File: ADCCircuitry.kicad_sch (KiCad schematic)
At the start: 24 parts, among them J1 Screw_Terminal_01x04, J2 Screw_Terminal_01x04, J3 Screw_Terminal_01x04, J4 Screw_Terminal_01x04, U2 ADS112C04, U3 ADS112C04, U4 ADS112C04, U5 ADS112C04

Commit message: Add SAFE +24V
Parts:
- J1, J2, J3, J4: Digikey PN (none) -> ED10563-ND
- TP1, TP2, TP3, TP4: footprint (none) -> TestPoint:TestPoint_Pad_D2.0mm
- U2, U3, U4, U5: LCSC (none) -> C701615; MPN (none) -> ADS112C04IPWR
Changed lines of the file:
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@@
 			)
 		)
-		(property "Footprint" ""
+		(property "Footprint" "TestPoint:TestPoint_Pad_D2.0mm"
 			(at 62.23 115.57 0)
 			(effects
@@
 			)
 		)
+		(property "Digikey PN" "ED10563-ND"
+			(at 201.93 40.64 0)
+			(effects
+				(font
+					(size 1.27 1.27)
+				)
+				(hide yes)
+			)
+		)
 		(pin "2"
 		)
@@
 			)
 		)
-		(property "Footprint" ""
+		(property "Footprint" "TestPoint:TestPoint_Pad_D2.0mm"
 			(at 62.23 64.77 0)
 			(effects
@@
 			)
 		)
-		(property "Footprint" ""
+		(property "Footprint" "TestPoint:TestPoint_Pad_D2.0mm"
 			(at 184.15 115.57 0)
 			(effects
@@
 			)
 		)
+		(property "MPN" "ADS112C04IPWR"
+			(at 99.06 134.62 0)
+			(effects
+				(font
+					(size 1.27 1.27)
+				)
+				(hide yes)
+			)
+		)
+		(property "LCSC" "C701615"
+			(at 99.06 134.62 0)
+			(effects
+				(font
+					(size 1.27 1.27)
+				)
+				(hide yes)
+			)
+		)
 		(property "ADC Number" "2"
 			(at 99.06 134.62 0)
@@
 			)
 		)
-		(property "Footprint" ""
+		(property "Footprint" "TestPoint:TestPoint_Pad_D2.0mm"
 			(at 184.15 64.77 0)
 			(effects
@@
 			)
 		)
+		(property "MPN" "ADS112C04IPWR"
+			(at 99.06 83.82 0)
+			(effects
+				(font
+					(size 1.27 1.27)
+				)
+				(hide yes)
+			)
+		)
+		(property "LCSC" "C701615"
+			(at 99.06 83.82 0)
+			(effects
+				(font
+					(size 1.27 1.27)
+				)
+				(hide yes)
+			)
+		)
 		(pin "2"
 		)
@@
 			)
 		)
+		(property "LCSC" "C701615"
+			(at 220.98 83.82 0)
+			(effects
+				(font
+					(size 1.27 1.27)
+				)
+				(hide yes)
+			)
+		)
+		(property "MPN" "ADS112C04IPWR"
+			(at 220.98 83.82 0)
+			(effects
+				(font
+					(size 1.27 1.27)
+				)
+				(hide yes)
+			)
+		)
 		(pin "2"
 		)
@@
 			)
 		)
+		(property "Digikey PN" "ED10563-ND"
+			(at 63.5 40.64 0)
+			(effects
+				(font
+					(size 1.27 1.27)
+				)
+				(hide yes)
+			)
+		)
 		(pin "2"
 		)
@@
 			)
 		)
+		(property "Digikey PN" "ED10563-ND"
+			(at 63.5 27.94 0)
+			(effects
+				(font
+					(size 1.27 1.27)
+				)
+				(hide yes)
+			)
+		)
 		(pin "2"
 		)
@@
 			)
 		)
+		(property "MPN" "ADS112C04IPWR"
+			(at 220.98 134.62 0)
+			(effects
+				(font
+					(size 1.27 1.27)
+				)
+				(hide yes)
+			)
+		)
+		(property "LCSC" "C701615"
+			(at 220.98 134.62 0)
+			(effects
+				(font
+					(size 1.27 1.27)
+				)
+				(hide yes)
+			)
+		)
 		(pin "2"
 		)
@@
 			(at 201.93 27.94 0)
 			(effects
+				(font
+					(size 1.27 1.27)
+				)
+				(hide yes)
+			)
+		)
+		(property "Digikey PN" "ED10563-ND"
+			(at 201.93 27.94 0)
+			(effects

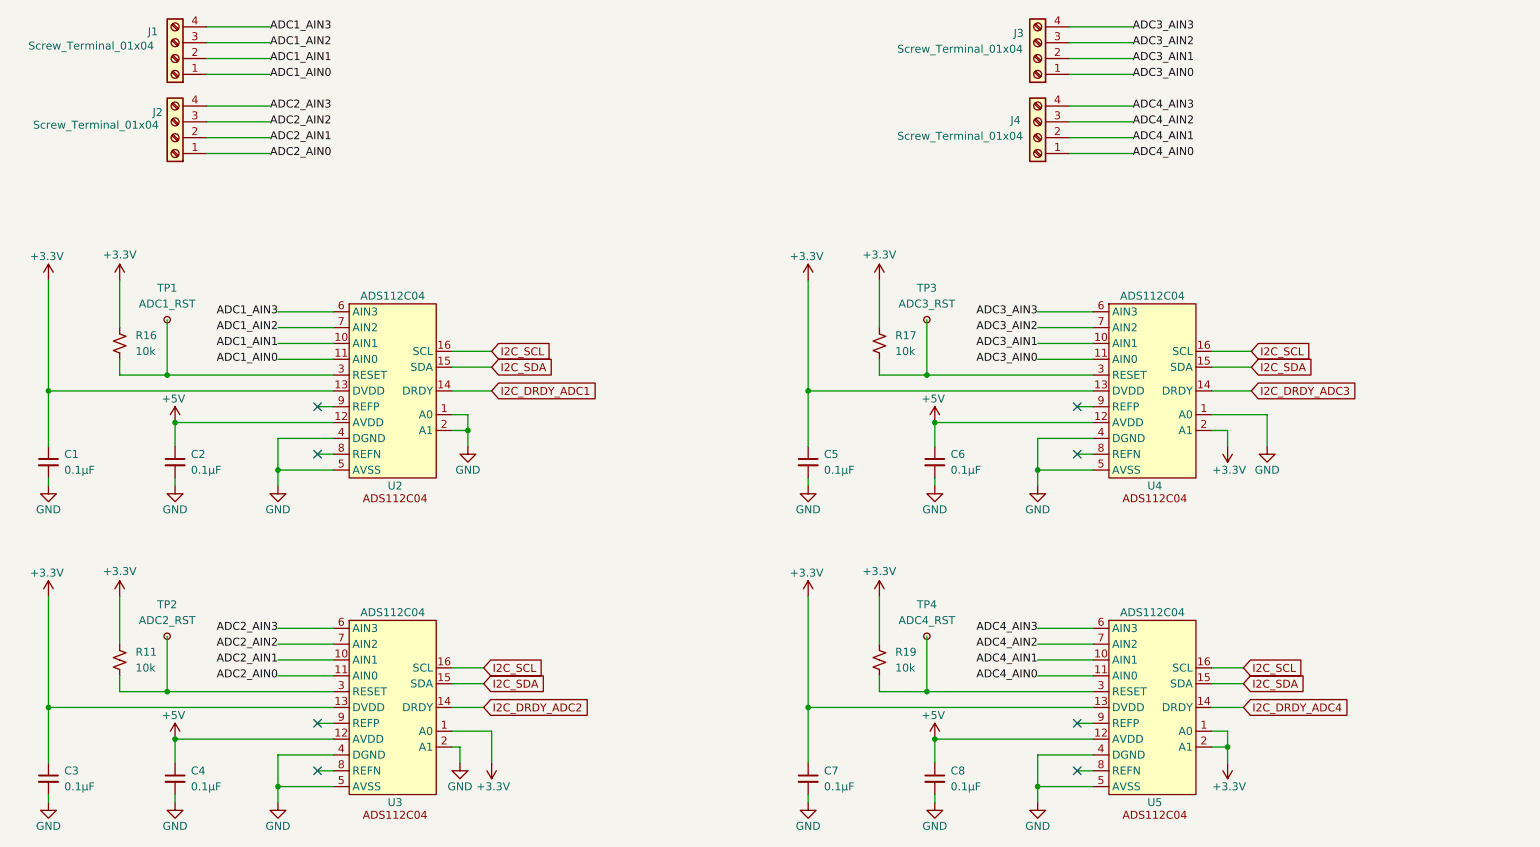
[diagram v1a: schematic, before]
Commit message: Add load cell inputs
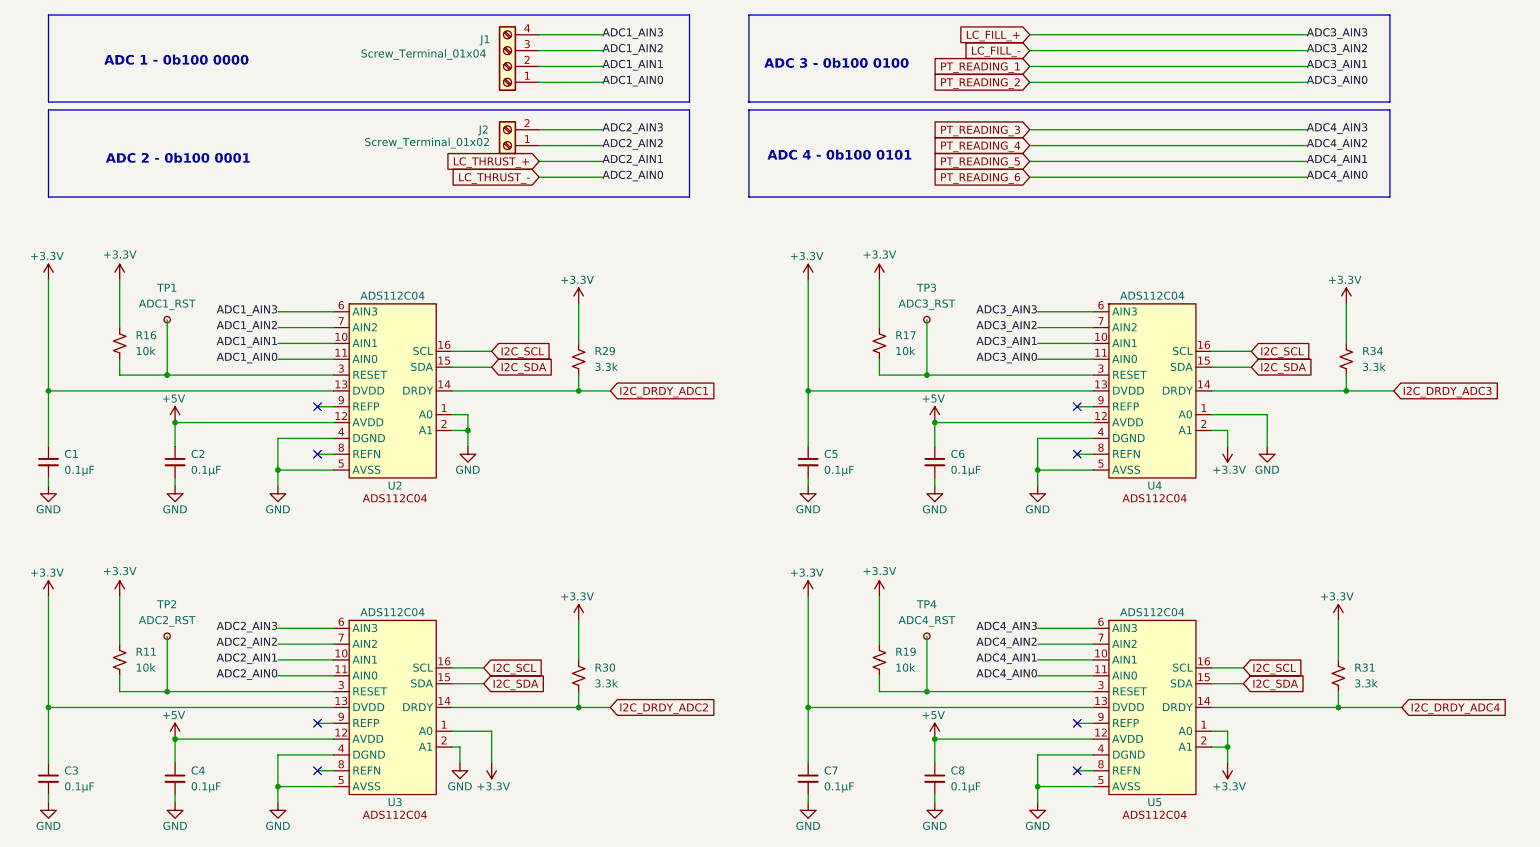
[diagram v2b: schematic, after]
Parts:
- removed J2, J3, J4: Screw_Terminal_01x04, TerminalBlock:TerminalBlock_Xinya_XY308-2.54-4P_1x04_P2.54mm_Horizontal, symbol Connector:Screw_Terminal_01x04
- added J2: Screw_Terminal_01x02, symbol Connector:Screw_Terminal_01x02
- added R29, R30, R31, R34: 3.3k, Resistor_SMD:R_0402_1005Metric, symbol Device:R_Small_US
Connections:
- net +3.3V: now also R29.1, R30.1, R31.1, R34.1
- net ADC2_AIN2: now also J2.1 (Pin_1)
- net ADC2_AIN3: now also J2.2 (Pin_2)
- net I2C_DRDY_ADC1: now also R29.2
- net I2C_DRDY_ADC2: now also R30.2
- net I2C_DRDY_ADC3: now also R34.2
- net I2C_DRDY_ADC4: now also R31.2
- net ADC2_AIN0 renamed LC_THRUST_-
- net ADC2_AIN1 renamed LC_THRUST_+
- net ADC3_AIN0 renamed PT_READING_2
- net ADC3_AIN1 renamed PT_READING_1
- net ADC3_AIN2 renamed LC_FILL_-
- net ADC3_AIN3 renamed LC_FILL_+
- net ADC4_AIN0 renamed PT_READING_6
- net ADC4_AIN1 renamed PT_READING_5
- net ADC4_AIN2 renamed PT_READING_4
- net ADC4_AIN3 renamed PT_READING_3
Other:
- note added: "ADC 1 - 0b100 0000"
- note added: "ADC 2 - 0b100 0001"
- note added: "ADC 3 - 0b100 0100"
- note added: "ADC 4 - 0b100 0101"
- moved on the sheet: J1

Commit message: v0.1 sch. Add devkit c1 footprint
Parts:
- J2: footprint (none) -> TerminalBlock:TerminalBlock_Xinya_XY308-2.54-2P_1x02_P2.54mm_Horizontal
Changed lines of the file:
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@@
 			)
 		)
-		(property "Footprint" ""
+		(property "Footprint" "TerminalBlock:TerminalBlock_Xinya_XY308-2.54-2P_1x02_P2.54mm_Horizontal"
 			(at 116.84 41.91 0)
 			(effects

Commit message: Add all footprints
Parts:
- U2, U3, U4, U5: footprint ADS112C04IPWR:SOP65P640X120-16N -> Package_SO:TSSOP-16_4.4x5mm_P0.65mm
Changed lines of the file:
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@@
 			)
 		)
-		(property "Footprint" "ADS112C04IPWR:SOP65P640X120-16N"
+		(property "Footprint" "Package_SO:TSSOP-16_4.4x5mm_P0.65mm"
 			(at 223.52 128.27 0)
 			(effects
@@
 			)
 		)
-		(property "Footprint" "ADS112C04IPWR:SOP65P640X120-16N"
+		(property "Footprint" "Package_SO:TSSOP-16_4.4x5mm_P0.65mm"
 			(at 223.52 77.47 0)
 			(effects
@@
 			)
 		)
-		(property "Footprint" "ADS112C04IPWR:SOP65P640X120-16N"
+		(property "Footprint" "Package_SO:TSSOP-16_4.4x5mm_P0.65mm"
 			(at 345.44 77.47 0)
 			(effects
@@
 			)
 		)
-		(property "Footprint" "ADS112C04IPWR:SOP65P640X120-16N"
+		(property "Footprint" "Package_SO:TSSOP-16_4.4x5mm_P0.65mm"
 			(at 345.44 128.27 0)
 			(effects

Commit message: Almost done routing
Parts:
- TP1, TP2, TP3, TP4: footprint TestPoint:TestPoint_Pad_D2.0mm -> TestPoint:TestPoint_Pad_D1.0mm
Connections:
- net PT_READING_3: now also U5.7 (AIN2); no longer U5.6 (AIN3)
- net PT_READING_4: now also U5.6 (AIN3); no longer U5.7 (AIN2)

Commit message: routing broken
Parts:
- removed TP1: ADC1_RST, TestPoint:TestPoint_Pad_D1.0mm, symbol Connector:TestPoint_Small
- removed TP2: ADC2_RST, TestPoint:TestPoint_Pad_D1.0mm, symbol Connector:TestPoint_Small
- removed TP3: ADC3_RST, TestPoint:TestPoint_Pad_D1.0mm, symbol Connector:TestPoint_Small
- removed TP4: ADC4_RST, TestPoint:TestPoint_Pad_D1.0mm, symbol Connector:TestPoint_Small
- renumbered C3 to C2, C2 to C3, C7 to C6, C6 to C7, J2 to J10, J1 to J9, R16 to R15, R11 to R16, R29 to R17, R30 to R18, R17 to R19, R19 to R20, R31 to R21, R34 to R22

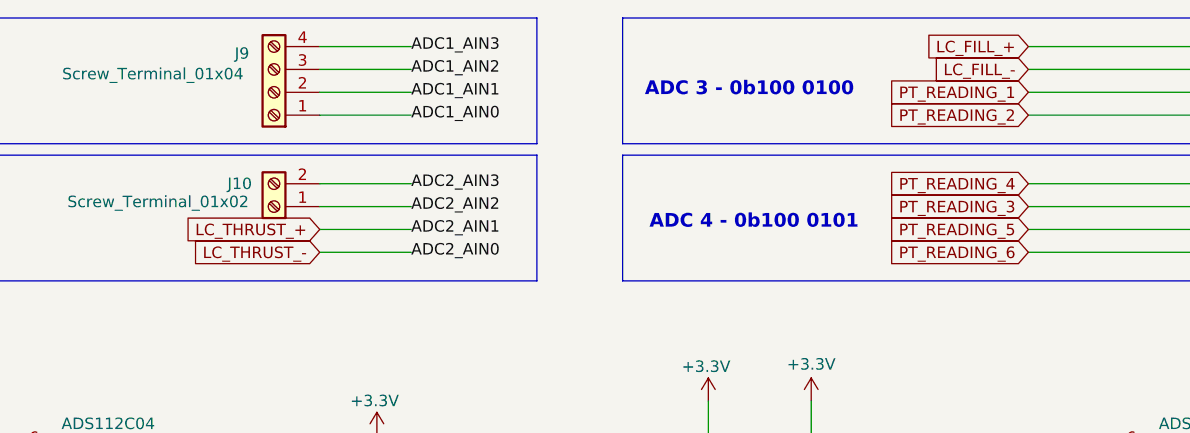
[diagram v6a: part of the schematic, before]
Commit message: Route power to sensors
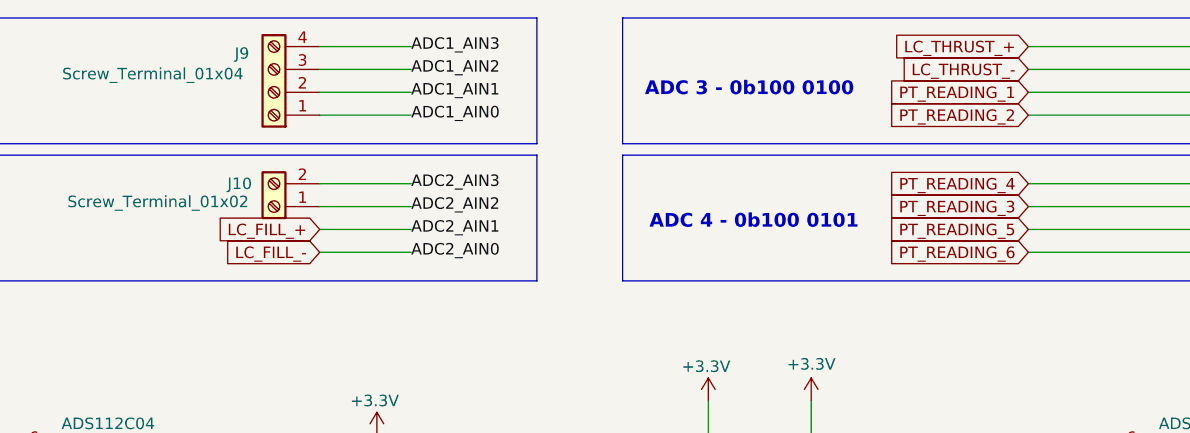
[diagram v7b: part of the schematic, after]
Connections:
- net LC_FILL_+: now also U3.10 (AIN1); no longer U4.6 (AIN3)
- net LC_FILL_-: now also U3.11 (AIN0); no longer U4.7 (AIN2)
- net LC_THRUST_+: now also U4.6 (AIN3); no longer U3.10 (AIN1)
- net LC_THRUST_-: now also U4.7 (AIN2); no longer U3.11 (AIN0)
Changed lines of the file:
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@@
+		)
+	)
+	(global_label "LC_THRUST_+"
+		(shape input)
+		(at 200.66 24.13 180)
+		(fields_autoplaced yes)
+		(effects
+			(font
+				(size 1.27 1.27)
+			)
+			(justify right)
+		)
+		(property "Intersheetrefs" "${INTERSHEET_REFS}"
+			(at 184.7934 24.13 0)
+			(effects
+				(font
+					(size 1.27 1.27)
+				)
+				(justify right)
+				(hide yes)
+			)
 		)
 	)
@@
 		)
 	)
-	(global_label "LC_THRUST_+"
+	(global_label "LC_THRUST_-"
+		(shape input)
+		(at 200.66 26.67 180)
+		(fields_autoplaced yes)
+		(effects
+			(font
+				(size 1.27 1.27)
+			)
+			(justify right)
+		)
+		(property "Intersheetrefs" "${INTERSHEET_REFS}"
+			(at 184.7934 26.67 0)
+			(effects
+				(font
+					(size 1.27 1.27)
+				)
+				(justify right)
+				(hide yes)
+			)
+		)
+	)
+	(global_label "LC_FILL_-"
+		(shape input)
+		(at 121.92 46.99 180)
+		(fields_autoplaced yes)
+		(effects
+			(font
+				(size 1.27 1.27)
+			)
+			(justify right)
+		)
+		(property "Intersheetrefs" "${INTERSHEET_REFS}"
+			(at 109.3795 46.99 0)
+			(effects
+				(font
+					(size 1.27 1.27)
+				)
+				(justify right)
+				(hide yes)
+			)
+		)
+	)
+	(global_label "PT_READING_2"
+		(shape input)
+		(at 200.66 31.75 180)
+		(fields_autoplaced yes)
+		(effects
+			(font
+				(size 1.27 1.27)
+			)
+			(justify right)
+		)
+		(property "Intersheetrefs" "${INTERSHEET_REFS}"
+			(at 184.3096 31.75 0)
+			(effects
+				(font
+					(size 1.27 1.27)
+				)
+				(justify right)
+				(hide yes)
+			)
+		)
+	)
+	(global_label "LC_FILL_+"
 		(shape input)
 		(at 121.92 44.45 180)
@@
 		)
 		(property "Intersheetrefs" "${INTERSHEET_REFS}"
-			(at 106.0534 44.45 0)
-			(effects
-				(font
-					(size 1.27 1.27)
-				)
-				(justify right)
-				(hide yes)
-			)
-		)
-	)
-	(global_label "LC_THRUST_-"
-		(shape input)
-		(at 121.92 46.99 180)
-		(fields_autoplaced yes)
-		(effects
-			(font
-				(size 1.27 1.27)
-			)
-			(justify right)
-		)
-		(property "Intersheetrefs" "${INTERSHEET_REFS}"
-			(at 106.0534 46.99 0)
-			(effects
-				(font
-					(size 1.27 1.27)
-				)
-				(justify right)
-				(hide yes)
-			)
-		)
-	)
-	(global_label "PT_READING_2"
-		(shape input)
-		(at 200.66 31.75 180)
-		(fields_autoplaced yes)
-		(effects
-			(font
-				(size 1.27 1.27)
-			)
-			(justify right)
-		)
-		(property "Intersheetrefs" "${INTERSHEET_REFS}"
-			(at 184.3096 31.75 0)
+			(at 109.3795 44.45 0)
 			(effects
 				(font
@@
 		)
 	)
-	(global_label "LC_FILL_-"
-		(shape input)
-		(at 200.66 26.67 180)
-		(fields_autoplaced yes)
-		(effects
-			(font
-				(size 1.27 1.27)
-			)
-			(justify right)
-		)
-		(property "Intersheetrefs" "${INTERSHEET_REFS}"
-			(at 188.1195 26.67 0)
-			(effects
-				(font
-					(size 1.27 1.27)
-				)
-				(justify right)
-				(hide yes)
-			)
-		)
-	)
 	(global_label "I2C_SDA"
 		(shape input)
@@
 				(hide yes)
 			)
-		)
-	)
-	(global_label "LC_FILL_+"
-		(shape input)
-		(at 200.66 24.13 180)
-		(fields_autoplaced yes)
-		(effects
-			(font
-				(size 1.27 1.27)
-			)
-			(justify right)
-		)
-		(property "Intersheetrefs" "${INTERSHEET_REFS}"
-			(at 188.1195 24.13 0)
-			(effects
-				(font
-					(size 1.27 1.27)
-				)
-				(justify right)
-				(hide yes)
-			)

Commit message: Fix silk screening
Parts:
- J10, J9: now left out of the parts list
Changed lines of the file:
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@@
 	(paper "A4")
 	(title_block
-		(rev "0.1.0")
+		(rev "1.0.0")
 		(company "Queen's Rocket Engineering Team")
 	)
@@
 		(unit 1)
 		(exclude_from_sim no)
-		(in_bom yes)
+		(in_bom no)
 		(on_board yes)
 		(dnp no)
@@
 		(unit 1)
 		(exclude_from_sim no)
-		(in_bom yes)
+		(in_bom no)
 		(on_board yes)
 		(dnp no)
